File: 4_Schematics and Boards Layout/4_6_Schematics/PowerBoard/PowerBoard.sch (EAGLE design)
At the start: 312 parts, among them U1 TPS562208DDCT, U10 TPS562208DDCT, U11 TPS562208DDCT, U12 TPS562208DDCT, U13 TPS562208DDCT, U14 TPS562208DDCT, U15 TPS562208DDCT, U16 TPS562208DDCT, U17 TPS562208DDCT, U18 LM2662MX/NOPB, U19 LM2662MX/NOPB, U2 TPS562208DDCT, U20 LM2662MX/NOPB, U21 LM2662MX/NOPB, U22 LM2662MX/NOPB, U23 ADM7151ACPZ-04-R7, U24 TPS562208DDCT, U25 ADM7151ACPZ-04-R7, U26 TPS562208DDCT, U27 ADM7151ACPZ-04-R7, U28 TPS562208DDCT, U29 ADM7151ACPZ-04-R7, U3 TPS562208DDCT, U30 ADM7151ACPZ-04-R7, U31 TPS562208DDCT, U32 TPS7A8300RGRR, U33 TPS562208DDCT, U34 TPS7A8300RGRR, U4 TPS562208DDCT, U5 ADM7151ACPZ-04-R7, U6 TPS562208DDCT, U7 TPS562208DDCT, U8 TPS562208DDCT, U9 TPS562208DDCT, X10 22-23-2021, X11 22-23-2021, X12 22-23-2021, X13 22-23-2021, X14 22-23-2021, X15 22-23-2021, X16 22-23-2021, X17 22-23-2021, X18 22-23-2021, X19 22-23-2021, X2 22-23-2021, X20 22-23-2021, X21 22-23-2021, X22 22-23-2021, X23 22-23-2021, X24 22-23-2021, X25 22-23-2021, X26 22-23-2021, X27 22-23-2021, X28 22-23-2021, X29 22-23-2021, X3 22-23-2021, X30 22-23-2021, X31 22-23-2021, X32 22-23-2021, X33 22-23-2021, X34 22-23-2021, X35 22-23-2021, X4 22-23-2021, X5 22-23-2021, X6 22-23-2021, X7 22-23-2021, X8 22-23-2021, X9 22-23-2021

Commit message: feat(hw): the 2.5 V rail source for bank 14 (Lane B B1.1, part 1 of 2)
Bank 14 has to reach 2.5 V before the ADC lanes can be LVDS_25, and the supply
has to come from somewhere.  A third TPS7A8300 -- the part that already regulates
twice on the power board (U32 = +3V3_ADTR, U34 = +3V3_XO) -- so the topology,
including the BIAS, NR/SS and SNS capacitors the device needs, is copied from a
working instance rather than designed here.

The set point is derived from the board's own 3.3 V instances, not from memory:

    3.3 V = VREF x (1 + 35.7k/11.5k)       -> VREF = 0.804 V
    2.5 V -> R1/R2 = 2.109; keep the board's 11.5k bottom -> R1 = 24.3k
    0.804 x (1 + 24.3/11.5) = 2.503 V

Capacitors mirror the existing rails' values and packages (22 uF in and out,
10 uF BIAS, 10 nF NR/SS, 10 nF SNS, all C0603); EN is tied to the input rail
because a configuration-bank supply must be up when the FPGA configures.  The
rail leaves the board on the same 2-pin Molex the other rails use, including
X34's two-instance supply-pin pattern.

Placement was searched for clearance from every existing element (a 20-pin LDO
anchored at >12 mm, the passives >=2.5 mm).  Verified: both files parse (572
parts / 322 elements), the rail's net membership matches between schematic and
board (U35 OUT/OUT_2/OUT_3 to pads 20/1/19, plus R59, C165 and the connector),
all three artifact gates green, and the new rail appears in interboard_rails.csv
as a cross-board rail.  The BOM keeps the repo's grouping: C164-C168 and R60 and
U35 join their existing value rows, and 24.3k is the one new row, using the
ERJ-P06 series and the code scheme of the 35.7k part already fitted.

Harmless on its own by design: bank 14 stays on 3.3 V and nothing consumes this
rail yet.  Part 2 -- the two translators, the six line splits and the VCCO_14
move -- is what actually changes the bank, and it has to land with this.
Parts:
- added C164, C165: 22µF, rcl:C-EUC0603
- added C166: 10µF, rcl:C-EUC0603
- added C167, C168: 10nF, rcl:C-EUC0603
- added R59: 24.3k, rcl:R-EU_M0805
- added R60: 11.5k, rcl:R-EU_M0805
- added U35: TPS7A8300RGRR, My_Library_RADAR:TPS7A8300RGRR
- added X36: 22-23-202122-23-2021, con-molex:22-23-202122-23-2021
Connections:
- new net +2V5_FPGA: C165.1, R59.1, U35.OUT, U35.OUT_2, U35.OUT_3, X36-1.S
- new net N$2V5_BIAS: C166.1, U35.BIAS
- new net N$2V5_FB: C168.2, R59.2, R60.1, U35.FB
- new net N$2V5_NRSS: C167.1, U35.NR/SS
- new net N$2V5_SNS: C168.1, U35.SNS
- net +5V0_5: now also C164.1, U35.EN, U35.IN, U35.IN_2, U35.IN_3
- net GND: now also C164.2, C165.2, C166.2, C167.2, R60.2, U35.EPAD, U35.GND, U35.GND_2, X36-2.S
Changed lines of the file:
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@@
 <part name="C162" library="rcl" library_urn="urn:adsk.eagle:library:334" deviceset="C-EU" device="C0603" package3d_urn="urn:adsk.eagle:package:23616/2" value="10nF"/>
 <part name="GND241" library="supply1" library_urn="urn:adsk.eagle:library:371" deviceset="GND" device=""/>
-<part name="C163" library="rcl" library_urn="urn:adsk.eagle:library:334" deviceset="C-EU" device="C0603" package3d_urn="urn:adsk.eagle:package:23616/2" value="10µF"/>
+<part name="C163" library="rcl" library_urn="urn:adsk.eagle:library:334" deviceset="C-EU" device="C0603" package3d_urn="urn:adsk.eagle:package:23616/2" value="10µF"/><part name="U35" library="My_Library_RADAR" deviceset="TPS7A8300RGRR" device=""/><part name="R59" library="rcl" deviceset="R-EU_" device="M0805" value="24.3k"/><part name="R60" library="rcl" deviceset="R-EU_" device="M0805" value="11.5k"/><part name="C164" library="rcl" deviceset="C-EU" device="C0603" value="22µF"/><part name="C165" library="rcl" deviceset="C-EU" device="C0603" value="22µF"/><part name="C166" library="rcl" deviceset="C-EU" device="C0603" value="10µF"/><part name="C167" library="rcl" deviceset="C-EU" device="C0603" value="10nF"/><part name="C168" library="rcl" deviceset="C-EU" device="C0603" value="10nF"/><part name="X36" library="con-molex" deviceset="22-23-2021" device="22-23-2021"/><part name="GND250" library="supply1" deviceset="GND" device=""/>
 <part name="GND242" library="supply1" library_urn="urn:adsk.eagle:library:371" deviceset="GND" device=""/>
 <part name="X4" library="con-molex" library_urn="urn:adsk.eagle:library:165" deviceset="22-23-2021" device="" package3d_urn="urn:adsk.eagle:package:8078633/1"/>
@@
 <attribute name="VALUE" x="515.62" y="256.54" size="1.778" layer="96"/>
 </instance>
-<instance part="U32" gate="A" x="589.28" y="266.7" smashed="yes">
+<instance part="U35" gate="G$1" x="169.8" y="136.8" smashed="yes"><attribute name="NAME" x="167.8" y="138.3" size="1.524" layer="95"/></instance><instance part="R59" gate="G$1" x="176.0" y="142.0" smashed="yes"><attribute name="NAME" x="174.0" y="143.5" size="1.524" layer="95"/></instance><instance part="R60" gate="G$1" x="180.0" y="148.0" smashed="yes"><attribute name="NAME" x="178.0" y="149.5" size="1.524" layer="95"/></instance><instance part="C164" gate="G$1" x="164.0" y="130.0" smashed="yes"><attribute name="NAME" x="162.0" y="131.5" size="1.524" layer="95"/></instance><instance part="C165" gate="G$1" x="182.0" y="130.0" smashed="yes"><attribute name="NAME" x="180.0" y="131.5" size="1.524" layer="95"/></instance><instance part="C166" gate="G$1" x="186.0" y="142.0" smashed="yes"><attribute name="NAME" x="184.0" y="143.5" size="1.524" layer="95"/></instance><instance part="C167" gate="G$1" x="190.0" y="148.0" smashed="yes"><attribute name="NAME" x="188.0" y="149.5" size="1.524" layer="95"/></instance><instance part="C168" gate="G$1" x="174.0" y="148.0" smashed="yes"><attribute name="NAME" x="172.0" y="149.5" size="1.524" layer="95"/></instance><instance part="X36" gate="G$1" x="192.0" y="134.3" smashed="yes"><attribute name="NAME" x="190.0" y="135.8" size="1.524" layer="95"/></instance><instance part="X36" gate="-2" x="192.0" y="131.76000000000002" smashed="yes"><attribute name="NAME" x="190.0" y="131.0" size="1.524" layer="95"/></instance><instance part="GND250" gate="1" x="170" y="150" smashed="yes"><attribute name="VALUE" x="171" y="151" size="1.778" layer="96"/></instance><instance part="U32" gate="A" x="589.28" y="266.7" smashed="yes">
 <attribute name="NAME" x="607.4156" y="275.8186" size="2.0828" layer="95" ratio="6" rot="SR0"/>
 <attribute name="VALUE" x="606.7806" y="273.2786" size="2.0828" layer="96" ratio="6" rot="SR0"/>
@@
 <busses>
 </busses>
-<nets>
+<nets><net name="N$2V5_NRSS" class="0"><segment><pinref part="U35" gate="G$1" pin="NR/SS"/><pinref part="C167" gate="G$1" pin="1"/></segment></net><net name="N$2V5_BIAS" class="0"><segment><pinref part="U35" gate="G$1" pin="BIAS"/><pinref part="C166" gate="G$1" pin="1"/></segment></net><net name="N$2V5_SNS" class="0"><segment><pinref part="U35" gate="G$1" pin="SNS"/><pinref part="C168" gate="G$1" pin="1"/></segment></net><net name="N$2V5_FB" class="0"><segment><pinref part="U35" gate="G$1" pin="FB"/><pinref part="R59" gate="G$1" pin="2"/><pinref part="R60" gate="G$1" pin="1"/><pinref part="C168" gate="G$1" pin="2"/></segment></net><net name="+2V5_FPGA" class="0"><segment><pinref part="U35" gate="G$1" pin="OUT"/><pinref part="U35" gate="G$1" pin="OUT_2"/><pinref part="U35" gate="G$1" pin="OUT_3"/><pinref part="R59" gate="G$1" pin="1"/><pinref part="C165" gate="G$1" pin="1"/><pinref part="X36" gate="-1" pin="S"/></segment></net>
 <net name="GND" class="0">
 <segment>
@@
 <pinref part="X35" gate="-2" pin="S"/>
 <pinref part="GND249" gate="1" pin="GND"/>
-</segment>
+<pinref part="U35" gate="G$1" pin="GND"/><pinref part="U35" gate="G$1" pin="GND_2"/><pinref part="U35" gate="G$1" pin="EPAD"/><pinref part="R60" gate="G$1" pin="2"/><pinref part="C164" gate="G$1" pin="2"/><pinref part="C165" gate="G$1" pin="2"/><pinref part="C166" gate="G$1" pin="2"/><pinref part="C167" gate="G$1" pin="2"/><pinref part="X36" gate="-2" pin="S"/><pinref part="GND250" gate="1" pin="GND"/></segment>
 </net>
 <net name="N$1" class="0">
@@
 <wire x1="802.64" y1="375.92" x2="795.02" y2="375.92" width="0.1524" layer="91"/>
 <junction x="795.02" y="375.92"/>
-</segment>
+<pinref part="U35" gate="G$1" pin="IN"/><pinref part="U35" gate="G$1" pin="IN_2"/><pinref part="U35" gate="G$1" pin="IN_3"/><pinref part="U35" gate="G$1" pin="EN"/><pinref part="C164" gate="G$1" pin="1"/></segment>
 </net>
 <net name="+3V3_XO" class="0">

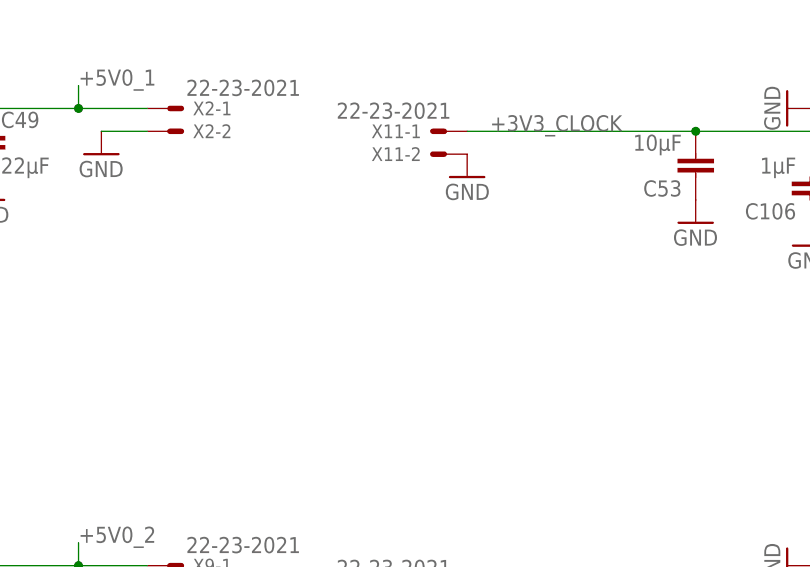
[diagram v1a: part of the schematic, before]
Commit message: fix(hw): stale sense-amp annotation, and +3V3_XO bulk (Lane B B3.5)
Two grounded fixes, both from the progress audit rather than from the tracker's word.

1. Stale annotation. The main-board sheet has read "6 X INA241A3" twice since before this
   work: once wrong in the part (B2.5 made every sense amplifier an INA241A4) and once
   wrong in the count (the netlist has 16 of them). They sit in two columns of 8
   (U11,U73-U79 at x=419.10 and U80-U87 at x=650.24), so each label annotates one column:
   now "8 X INA241A4" twice, and 2 x 8 = the 16 in the netlist. The neighbouring labels
   ("2 X DAC5578", "3 X ADS7830") already match the netlist, which is the check that made
   this one's staleness visible instead of assumed.

2. B3.5 -- +3V3_XO. Steady state is ~1.25 A (1.2 A OCXO) on a 3 A TPS7A8300: 42 %, fine.
   Added four 22 uF C0603 (C169-C172) on the rail, reusing the part the board already
   carries -- the same BOM row and MPN (KGM15CR51E226MT, qty 54 -> 58) rather than a new
   line. This cuts the rail's source impedance at the heater's step load.

   What it does NOT do, stated plainly: cover a cold-start inrush. A capacitor holds a rail
   for t = C*dV/dI, so the ~32 uF now fitted buys microseconds, not milliseconds. The
   OCXO's inrush current is in no vendor source reachable from here (the part has no
   findable datasheet), so the cold-start capture remains a bench step -- and if it exceeds
   the regulator's 3 A, the fixes are sequencing (U34.EN is tied to +5V0_5 today, so that
   costs an MCU pin) or a soft-start, not more bulk.

Verified: both files parse; all four caps are on +3V3_XO and GND in schematic *and* board;
BOM row is 58 unique refs with all four present; no duplicate designators introduced; three
artifact gates exit 0.

Recorded while checking, not fixed (no decidable answer in the files):
  * X36 appears twice as a board element on the power board -- two connectors, one refdes,
    pre-existing at HEAD. Real BOM/assembly ambiguity, unde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
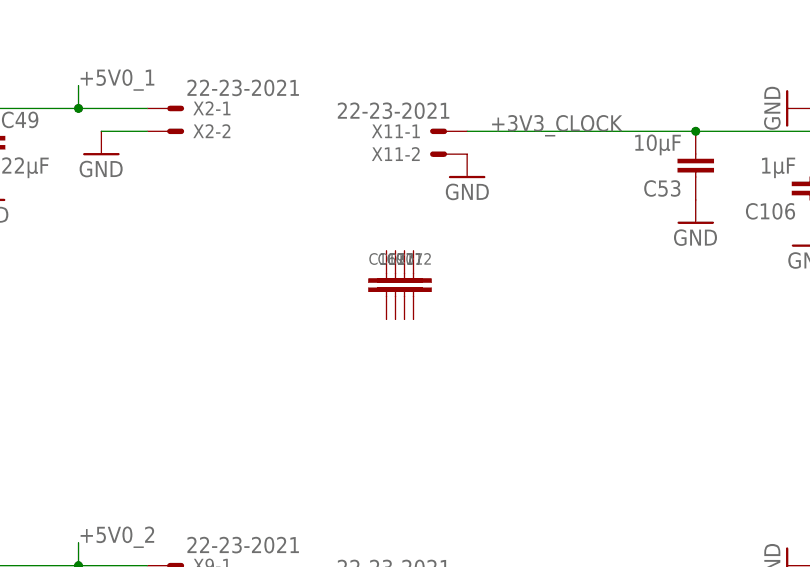
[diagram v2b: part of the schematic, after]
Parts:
- added C169, C170, C171, C172: 22µF, rcl:C-EUC0603
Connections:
- net +3V3_XO: now also C169.1, C170.1, C171.1, C172.1
- net GND: now also C169.2, C170.2, C171.2, C172.2
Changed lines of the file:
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@@
 <part name="GND236" library="supply1" library_urn="urn:adsk.eagle:library:371" deviceset="GND" device=""/>
 <part name="GND237" library="supply1" library_urn="urn:adsk.eagle:library:371" deviceset="GND" device=""/>
-<part name="C159" library="rcl" library_urn="urn:adsk.eagle:library:334" deviceset="C-EU" device="C0603" package3d_urn="urn:adsk.eagle:package:23616/2" value="22µF"/>
+<part name="C169" library="rcl" deviceset="C-EU" device="C0603" value="22µF"/><part name="C170" library="rcl" deviceset="C-EU" device="C0603" value="22µF"/><part name="C171" library="rcl" deviceset="C-EU" device="C0603" value="22µF"/><part name="C172" library="rcl" deviceset="C-EU" device="C0603" value="22µF"/><part name="C159" library="rcl" library_urn="urn:adsk.eagle:library:334" deviceset="C-EU" device="C0603" package3d_urn="urn:adsk.eagle:package:23616/2" value="22µF"/>
 <part name="GND238" library="supply1" library_urn="urn:adsk.eagle:library:371" deviceset="GND" device=""/>
 <part name="C160" library="rcl" library_urn="urn:adsk.eagle:library:334" deviceset="C-EU" device="C0603" package3d_urn="urn:adsk.eagle:package:23616/2" value="10nF"/>
@@
 <attribute name="VALUE" x="800.1" y="314.96" size="1.778" layer="96"/>
 </instance>
-<instance part="C159" gate="G$1" x="787.4" y="294.64" smashed="yes" rot="R90">
+<instance part="C169" gate="G$1" x="191.7" y="283.9" smashed="yes"><attribute name="NAME" x="189.7" y="284.9" size="1.27" layer="95"/></instance><instance part="C170" gate="G$1" x="192.7" y="283.9" smashed="yes"><attribute name="NAME" x="190.7" y="284.9" size="1.27" layer="95"/></instance><instance part="C171" gate="G$1" x="193.7" y="283.9" smashed="yes"><attribute name="NAME" x="191.7" y="284.9" size="1.27" layer="95"/></instance><instance part="C172" gate="G$1" x="194.7" y="283.9" smashed="yes"><attribute name="NAME" x="192.7" y="284.9" size="1.27" layer="95"/></instance><instance part="C159" gate="G$1" x="787.4" y="294.64" smashed="yes" rot="R90">
 <attribute name="NAME" x="787.019" y="296.164" size="1.778" layer="95" rot="R90"/>
 <attribute name="VALUE" x="792.099" y="296.164" size="1.778" layer="96" rot="R90"/>
@@
 <pinref part="X35" gate="-2" pin="S"/>
 <pinref part="GND249" gate="1" pin="GND"/>
-<pinref part="U35" gate="G$1" pin="GND"/><pinref part="U35" gate="G$1" pin="GND_2"/><pinref part="U35" gate="G$1" pin="EPAD"/><pinref part="R60" gate="G$1" pin="2"/><pinref part="C164" gate="G$1" pin="2"/><pinref part="C165" gate="G$1" pin="2"/><pinref part="C166" gate="G$1" pin="2"/><pinref part="C167" gate="G$1" pin="2"/><pinref part="X36" gate="-2" pin="S"/><pinref part="GND250" gate="1" pin="GND"/></segment>
+<pinref part="U35" gate="G$1" pin="GND"/><pinref part="U35" gate="G$1" pin="GND_2"/><pinref part="U35" gate="G$1" pin="EPAD"/><pinref part="R60" gate="G$1" pin="2"/><pinref part="C164" gate="G$1" pin="2"/><pinref part="C165" gate="G$1" pin="2"/><pinref part="C166" gate="G$1" pin="2"/><pinref part="C167" gate="G$1" pin="2"/><pinref part="X36" gate="-2" pin="S"/><pinref part="GND250" gate="1" pin="GND"/><pinref part="C169" gate="G$1" pin="2"/><pinref part="C170" gate="G$1" pin="2"/><pinref part="C171" gate="G$1" pin="2"/><pinref part="C172" gate="G$1" pin="2"/></segment>
 </net>
 <net name="N$1" class="0">
@@
 <pinref part="X35" gate="-1" pin="S"/>
 <wire x1="800.1" y1="287.02" x2="800.1" y2="281.94" width="0.1524" layer="91"/>
-</segment>
+<pinref part="C169" gate="G$1" pin="1"/><pinref part="C170" gate="G$1" pin="1"/><pinref part="C171" gate="G$1" pin="1"/><pinref part="C172" gate="G$1" pin="1"/></segment>
 </net>
 </nets>
